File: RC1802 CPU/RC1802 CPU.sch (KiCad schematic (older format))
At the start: 65 parts, among them J1 CONN_01X39, J2 BARREL_JACK, J3 Mount, J4 Mount, J5 Mount, J6 Mount, SW1 CLEAR, SW10 IN5, SW11 IN6, SW12 IN7, SW2 IN, SW3 MP, SW4 WAIT, SW5 IN0, SW6 IN1, SW7 IN2, SW8 IN3, SW9 IN4, U1 CDP1802, U10 MC14495P1, U11 28C256, U2 74LS373, U3 HM62256BLP-7, U4 74LS04, U5 4050, U6 4013, U7 74LS10, U8 MC14495P1, U9 74LS245, X1 CXO_DIP14

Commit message: Placed PCB components (no tracks)
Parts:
- removed AFF1: MSB, Displays_7-Segment:7SegmentLED_LTS6760_LTS6780, symbol LTS-6980HR
- removed AFF2: LSB, Displays_7-Segment:7SegmentLED_LTS6760_LTS6780, symbol LTS-6980HR
- removed C10, C11, C7, C8, C9: 100nF, Capacitors_THT:C_Disc_D4.7mm_W2.5mm_P5.00mm, symbol C_Small
- removed D1: Q LED, LEDs:LED_D5.0mm, symbol LED
- removed D2, D3, D4, D5, D6, D7: 1N4848, Diodes_THT:D_DO-35_SOD27_P7.62mm_Horizontal, symbol D
- removed RN1: 100k, Resistors_THT:R_Array_SIP9, symbol R_Network08
- removed SW1: CLEAR, switches:SPDT_SWITCH, symbol SW_SPDT
- removed SW10: IN5, switches:SPDT_SWITCH, symbol SW_Push_SPDT
- removed SW11: IN6, switches:SPDT_SWITCH, symbol SW_Push_SPDT
- removed SW12: IN7, switches:SPDT_SWITCH, symbol SW_Push_SPDT
- removed SW2: IN, switches:SPDT_PUSH, symbol SW_Push_SPDT
- removed SW3: MP, switches:SPDT_SWITCH, symbol SW_SPDT
- removed SW4: WAIT, switches:SPDT_SWITCH, symbol SW_SPDT
- removed SW5: IN0, switches:SPDT_SWITCH, symbol SW_Push_SPDT
- removed SW6: IN1, switches:SPDT_SWITCH, symbol SW_Push_SPDT
- removed SW7: IN2, switches:SPDT_SWITCH, symbol SW_Push_SPDT
- removed SW8: IN3, switches:SPDT_SWITCH, symbol SW_Push_SPDT
- removed SW9: IN4, switches:SPDT_SWITCH, symbol SW_Push_SPDT
- removed U10, U8: MC14495P1, Housings_DIP:DIP-16_W7.62mm_Socket, symbol MC14495P1
- removed U4: 74LS04, Housings_DIP:DIP-14_W7.62mm_Socket, symbol 74LS04
- removed U5: 4050, Housings_DIP:DIP-16_W7.62mm_Socket, symbol 4050
- removed U6: 4013, Housings_DIP:DIP-14_W7.62mm_Socket, symbol 4013
- removed U7: 74LS10, Housings_DIP:DIP-14_W7.62mm_Socket, symbol 74LS10
- removed U9: 74LS245, Housings_DIP:DIP-20_W7.62mm_Socket, symbol 74HC245
- added D1, D2, D3, D4, D5, D6, D7, D8: LED_Small, LEDs:LED_D5.0mm, symbol LED_Small
- added J6: CONN_02X20, Pin_Headers:Pin_Header_Straight_2x20_Pitch2.54mm, symbol CONN_02X20
- added JP5: SLOT1_WE, Pin_Headers:Pin_Header_Straight_1x03_Pitch2.54mm, symbol Jumper_NC_Dual
- added JP6: BM_OE, Pin_Headers:Pin_Header_Straight_1x03_Pitch2.54mm, symbol Jumper_NC_Dual
- added R11, R12, R13, R14, R15: 220, Resistors_THT:R_Axial_DIN0207_L6.3mm_D2.5mm_P10.16mm_Horizontal, symbol R
- added U1: 74LS04, Housings_DIP:DIP-14_W7.62mm_Socket, symbol 74LS04
- added U3: 74LS240, Housings_DIP:DIP-20_W7.62mm_Socket, symbol 74LS240
- JP4: renamed from JP1; value U12 WE -> SLOT2_WE
- R10: value 470 -> 220
- R8, R9: value 47k -> 220
- U5: renamed from U3; value HM62256BLP-7 -> SLOT-1
- U6: renamed from U11; value 28C256 -> SLOT-2
- renumbered J3 to J1, J4 to J2, J5 to J3, J6 to J4, J1 to J5, J2 to J7, JP2 to JP1, JP3 to JP2, JP4 to JP3, U1 to U2, U2 to U4
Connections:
- net labels added: MP, SLOT1_CS, SLOT2_CS, ~CLEAR, ~WAIT
- net labels removed: CS_RAM, CS_ROM, LOAD_N2, READ, STROBE, ~IN
- wire segments 297 -> 205
- no-connect marks 15 -> 13
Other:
- moved on the sheet: C1, C2, C3, C4, C5, J1, J2, J3, J4, J5, J7, JP1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

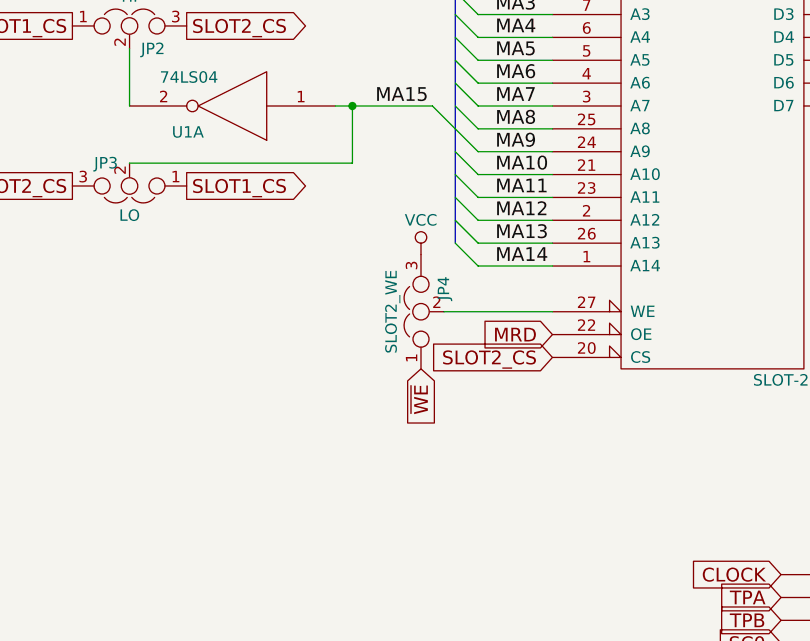
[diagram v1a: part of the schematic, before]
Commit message: All tracks layed out
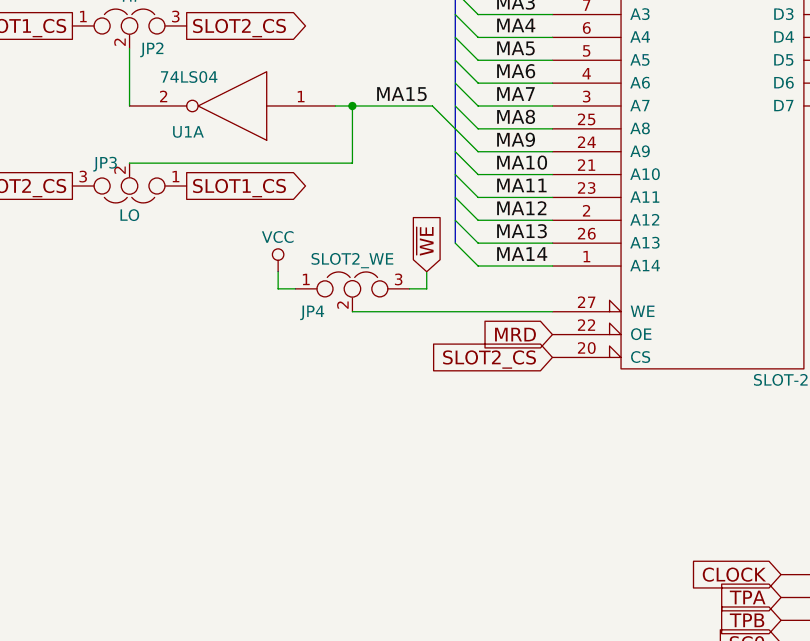
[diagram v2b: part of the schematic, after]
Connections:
- net VCC: now also JP4.1; no longer JP4.3
- net ~WE: now also JP4.3; no longer JP4.1
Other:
- moved on the sheet: JP4
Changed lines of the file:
@@
 L Jumper_NC_Dual JP4
 U 1 1 595437E7
-P 6175 6100
-F 0 "JP4" H 6225 6000 50  0000 L CNN
-F 1 "SLOT2_WE" H 6175 6200 50  0000 C BNN
-F 2 "Pin_Headers:Pin_Header_Straight_1x03_Pitch2.54mm" H 6175 6100 50  0001 C CNN
-F 3 "" H 6175 6100 50  0001 C CNN
-	1    6175 6100
-	0    -1   -1   0
+P 5875 6000
+F 0 "JP4" H 5650 5900 50  0000 L CNN
+F 1 "SLOT2_WE" H 5875 6100 50  0000 C BNN
+F 2 "Pin_Headers:Pin_Header_Straight_1x03_Pitch2.54mm" H 5875 6000 50  0001 C CNN
+F 3 "" H 5875 6000 50  0001 C CNN
+	1    5875 6000
+	1    0    0    -1
 $EndComp
 $Comp
 L VCC #PWR8
 U 1 1 59544DC9
-P 6175 5850
-F 0 "#PWR8" H 6175 5700 50  0001 C CNN
-F 1 "VCC" H 6175 6000 50  0000 C CNN
-F 2 "" H 6175 5850 50  0001 C CNN
-F 3 "" H 6175 5850 50  0001 C CNN
-	1    6175 5850
-	1    0    0    -1
-$EndComp
-Text GLabel 6175 6350 3    60   Input ~ 0
+P 5550 5925
+F 0 "#PWR8" H 5550 5775 50  0001 C CNN
+F 1 "VCC" H 5550 6075 50  0000 C CNN
+F 2 "" H 5550 5925 50  0001 C CNN
+F 3 "" H 5550 5925 50  0001 C CNN
+	1    5550 5925
+	1    0    0    -1
+$EndComp
+Text GLabel 6200 5925 1    60   Input ~ 0
 ~WE
 Text GLabel 15575 6400 0    60   Input ~ 0
@@
 	8750 2600 8525 2600
 Wire Wire Line
-	6275 6100 6750 6100
+	5875 6100 6750 6100
 Wire Wire Line
 	5800 5200 6225 5200
@@
 	11925 1300 11925 1250
 Connection ~ 11650 1300
+Wire Wire Line
+	6200 5925 6200 6000
+Wire Wire Line
+	6200 6000 6125 6000
+Wire Wire Line
+	5550 6000 5625 6000
+Wire Wire Line
+	5550 6000 5550 5925
 $EndSCHEMATC

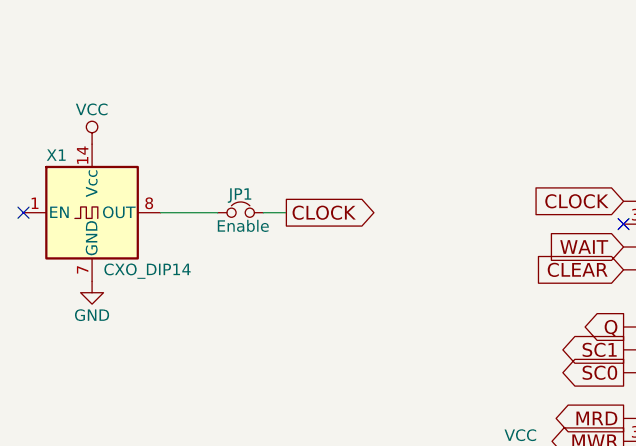
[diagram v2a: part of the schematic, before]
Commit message: Added provisions for using separate clock circuit
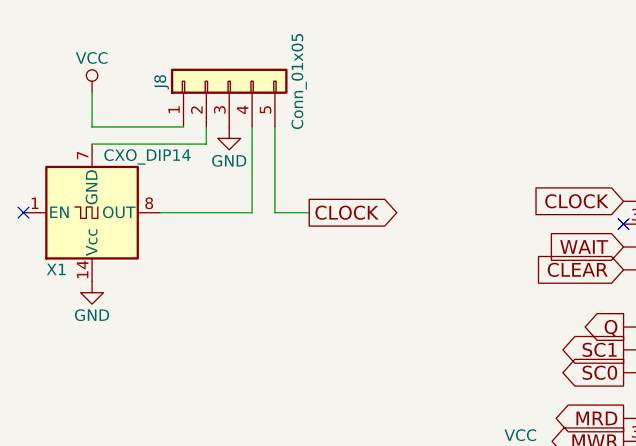
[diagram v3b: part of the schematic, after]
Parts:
- removed JP1: Enable, Pin_Headers:Pin_Header_Straight_1x02_Pitch2.54mm, symbol Jumper_NC_Small
- added J8: Conn_01x05, Pin_Headers:Pin_Header_Straight_1x05_Pitch2.54mm, symbol Conn_01x05
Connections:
- net CLOCK: now also J8.5 (Pin_5)
- net GND: now also X1.14 (Vcc), J8.3 (Pin_3); no longer X1.7 (GND)
- net VCC: now also J8.1 (Pin_1); no longer X1.14 (Vcc)
- net at X1.8 (OUT): now also J8.4 (Pin_4)
- new net: J8.2 (Pin_2), X1.7 (GND)
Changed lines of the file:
@@
 NoConn ~ 3425 1650
 $Comp
-L VCC #PWR21
+L VCC #PWR01
 U 1 1 5946201E
 P 15450 7600
-F 0 "#PWR21" H 15450 7450 50  0001 C CNN
+F 0 "#PWR01" H 15450 7450 50  0001 C CNN
 F 1 "VCC" H 15450 7750 50  0000 C CNN
 F 2 "" H 15450 7600 50  0001 C CNN
@@
 $EndComp
 $Comp
-L GND #PWR20
+L GND #PWR02
 U 1 1 5946208C
 P 15200 7500
-F 0 "#PWR20" H 15200 7250 50  0001 C CNN
+F 0 "#PWR02" H 15200 7250 50  0001 C CNN
 F 1 "GND" H 15200 7350 50  0000 C CNN
 F 2 "" H 15200 7500 50  0001 C CNN
@@
 $EndComp
 $Comp
-L VCC #PWR6
+L VCC #PWR03
 U 1 1 59462274
 P 4225 1075
-F 0 "#PWR6" H 4225 925 50  0001 C CNN
+F 0 "#PWR03" H 4225 925 50  0001 C CNN
 F 1 "VCC" H 4225 1225 50  0000 C CNN
 F 2 "" H 4225 1075 50  0001 C CNN
@@
 $EndComp
 $Comp
-L VCC #PWR7
+L VCC #PWR04
 U 1 1 594628A5
 P 5850 2200
-F 0 "#PWR7" H 5850 2050 50  0001 C CNN
+F 0 "#PWR04" H 5850 2050 50  0001 C CNN
 F 1 "VCC" H 5850 2350 50  0000 C CNN
 F 2 "" H 5850 2200 50  0001 C CNN
@@
 F 3 "" H 1000 1600 50  0001 C CNN
 	1    1100 1600
-	1    0    0    -1
-$EndComp
-$Comp
-L VCC #PWR1
+	1    0    0    1
+$EndComp
+$Comp
+L VCC #PWR05
 U 1 1 59462E75
-P 1100 1300
-F 0 "#PWR1" H 1100 1150 50  0001 C CNN
-F 1 "VCC" H 1100 1450 50  0000 C CNN
-F 2 "" H 1100 1300 50  0001 C CNN
-F 3 "" H 1100 1300 50  0001 C CNN
-	1    1100 1300
-	1    0    0    -1
-$EndComp
-$Comp
-L GND #PWR2
+P 1100 1075
+F 0 "#PWR05" H 1100 925 50  0001 C CNN
+F 1 "VCC" H 1100 1225 50  0000 C CNN
+F 2 "" H 1100 1075 50  0001 C CNN
+F 3 "" H 1100 1075 50  0001 C CNN
+	1    1100 1075
+	1    0    0    -1
+$EndComp
+$Comp
+L GND #PWR06
 U 1 1 59462F59
 P 1100 1900
-F 0 "#PWR2" H 1100 1650 50  0001 C CNN
+F 0 "#PWR06" H 1100 1650 50  0001 C CNN
 F 1 "GND" H 1100 1750 50  0000 C CNN
 F 2 "" H 1100 1900 50  0001 C CNN
@@
 EF4
 $Comp
-L VCC #PWR3
+L VCC #PWR07
 U 1 1 59464C11
 P 2975 2725
-F 0 "#PWR3" H 2975 2575 50  0001 C CNN
+F 0 "#PWR07" H 2975 2575 50  0001 C CNN
 F 1 "VCC" H 2975 2875 50  0000 C CNN
 F 2 "" H 2975 2725 50  0001 C CNN
@@
 TPA
 $Comp
-L GND #PWR9
+L GND #PWR08
 U 1 1 5946BB58
 P 6725 2300
-F 0 "#PWR9" H 6725 2050 50  0001 C CNN
+F 0 "#PWR08" H 6725 2050 50  0001 C CNN
 F 1 "GND" H 6725 2150 50  0000 C CNN
 F 2 "" H 6725 2300 50  0001 C CNN
@@
 BUS
 $Comp
-L GND #PWR5
+L GND #PWR09
 U 1 1 59474506
 P 4125 4300
-F 0 "#PWR5" H 4125 4050 50  0001 C CNN
+F 0 "#PWR09" H 4125 4050 50  0001 C CNN
 F 1 "GND" H 4125 4150 50  0000 C CNN
 F 2 "" H 4125 4300 50  0001 C CNN
@@
 Text Label 8125 2000 0    60   ~ 0
 MA15
-Text GLabel 1950 1600 2    60   Output ~ 0
+Text GLabel 2050 1600 2    60   Output ~ 0
 CLOCK
 Text GLabel 3425 1550 0    60   Input ~ 0
@@
 $EndComp
 $Comp
-L VCC #PWR8
+L VCC #PWR010
 U 1 1 59544DC9
 P 5550 5925
-F 0 "#PWR8" H 5550 5775 50  0001 C CNN
+F 0 "#PWR010" H 5550 5775 50  0001 C CNN
 F 1 "VCC" H 5550 6075 50  0000 C CNN
 F 2 "" H 5550 5925 50  0001 C CNN
@@
 SLOT1_CS
 $Comp
-L Jumper_NC_Small JP1
-U 1 1 5958558E
-P 1750 1600
-F 0 "JP1" H 1750 1680 50  0000 C CNN
-F 1 "Enable" H 1760 1540 50  0000 C CNN
-F 2 "Pin_Headers:Pin_Header_Straight_1x02_Pitch2.54mm" H 1750 1600 50  0001 C CNN
-F 3 "" H 1750 1600 50  0001 C CNN
-	1    1750 1600
-	1    0    0    -1
-$EndComp
-$Comp
 L C_Small C1
 U 1 1 595CF017
@@
 $EndComp
 $Comp
-L VCC #PWR14
+L VCC #PWR011
 U 1 1 595D67C5
 P 10550 950
-F 0 "#PWR14" H 10550 800 50  0001 C CNN
+F 0 "#PWR011" H 10550 800 50  0001 C CNN
 F 1 "VCC" H 10550 1100 50  0000 C CNN
 F 2 "" H 10550 950 50  0001 C CNN
@@
 $EndComp
 $Comp
-L GND #PWR15
+L GND #PWR012
 U 1 1 595D6DCD
 P 10550 1350
-F 0 "#PWR15" H 10550 1100 50  0001 C CNN
+F 0 "#PWR012" H 10550 1100 50  0001 C CNN
 F 1 "GND" H 10550 1200 50  0000 C CNN
 F 2 "" H 10550 1350 50  0001 C CNN
@@
 $EndComp
 $Comp
-L VCC #PWR22
+L VCC #PWR013
 U 1 1 595E10E8
 P 15575 1025
-F 0 "#PWR22" H 15575 875 50  0001 C CNN
+F 0 "#PWR013" H 15575 875 50  0001 C CNN
 F 1 "VCC" H 15575 1175 50  0000 C CNN
 F 2 "" H 15575 1025 50  0001 C CNN
@@
 $EndComp
 $Comp
-L GND #PWR23
+L GND #PWR014
 U 1 1 595E22B1
 P 15575 1400
-F 0 "#PWR23" H 15575 1150 50  0001 C CNN
+F 0 "#PWR014" H 15575 1150 50  0001 C CNN
 F 1 "GND" H 15575 1250 50  0000 C CNN
 F 2 "" H 15575 1400 50  0001 C CNN
@@
 	8125 2000 8325 2000
 Wire Wire Line
-	1400 1600 1650 1600
+	1400 1600 1800 1600
 Wire Bus Line
 	15050 8325 14850 8325
@@
 Wire Wire Line
 	4900 5450 5875 5450
-Wire Wire Line
-	1850 1600 1950 1600
 Wire Wire Line
 	10550 950  10550 1050
@@
 DMA_IN
 $Comp
-L VCC #PWR18
+L VCC #PWR015
 U 1 1 5987AAE8
 P 12875 3425
-F 0 "#PWR18" H 12875 3275 50  0001 C CNN
+F 0 "#PWR015" H 12875 3275 50  0001 C CNN
 F 1 "VCC" H 12875 3575 50  0000 C CNN
 F 2 "" H 12875 3425 50  0001 C CNN
@@
 $EndComp
 $Comp
-L GND #PWR19
+L GND #PWR016
 U 1 1 5987AAE9
 P 12950 5400
-F 0 "#PWR19" H 12950 5150 50  0001 C CNN
+F 0 "#PWR016" H 12950 5150 50  0001 C CNN
 F 1 "GND" H 12950 5250 50  0000 C CNN
 F 2 "" H 12950 5400 50  0001 C CNN
@@
 Connection ~ 1550 10000
 $Comp
-L GND #PWR4
+L GND #PWR017
 U 1 1 5B2329DF
 P 3000 10150
-F 0 "#PWR4" H 3000 9900 50  0001 C CNN
+F 0 "#PWR017" H 3000 9900 50  0001 C CNN
 F 1 "GND" H 3000 10000 50  0000 C CNN
 F 2 "" H 3000 10150 50  0001 C CNN
@@
 $EndComp
 $Comp
-L VCC #PWR12
+L VCC #PWR018
 U 1 1 5B230CC5
 P 8850 3300
-F 0 "#PWR12" H 8850 3150 50  0001 C CNN
+F 0 "#PWR018" H 8850 3150 50  0001 C CNN
 F 1 "VCC" H 8850 3450 50  0000 C CNN
 F 2 "" H 8850 3300 50  0001 C CNN
@@
 Connection ~ 7675 8200
 $Comp
-L VCC #PWR10
+L VCC #PWR019
 U 1 1 5B238BC7
 P 7275 8350
-F 0 "#PWR10" H 7275 8200 50  0001 C CNN
+F 0 "#PWR019" H 7275 8200 50  0001 C CNN
 F 1 "VCC" H 7275 8500 50  0000 C CNN
 F 2 "" H 7275 8350 50  0001 C CNN
@@
 $EndComp
 $Comp
-L GND #PWR11
+L GND #PWR020
 U 1 1 5B238E91
 P 7775 8350
-F 0 "#PWR11" H 7775 8100 50  0001 C CNN
+F 0 "#PWR020" H 7775 8100 50  0001 C CNN
 F 1 "GND" H 7775 8200 50  0000 C CNN
 F 2 "" H 7775 8350 50  0001 C CNN
@@
 $EndComp
 $Comp
-L GND #PWR13
+L GND #PWR021
 U 1 1 5B244389
 P 9725 8025
-F 0 "#PWR13" H 9725 7775 50  0001 C CNN
+F 0 "#PWR021" H 9725 7775 50  0001 C CNN
 F 1 "GND" H 9725 7875 50  0000 C CNN
 F 2 "" H 9725 8025 50  0001 C CNN
@@
 Wire Wire Line
 	5550 6000 5550 5925
+Wire Wire Line
+	1100 1300 1600 1300
+Wire Wire Line
+	1600 1300 1600 1225
+Wire Wire Line
+	1500 1225 1100 1225
+Wire Wire Line
+	1100 1225 1100 1075
+$Comp
+L Conn_01x05 J8
+U 1 1 5B2BCE80
+P 1700 1025
+F 0 "J8" H 1700 1325 50  0000 C CNN
+F 1 "Conn_01x05" H 1700 725 50  0000 C CNN
+F 2 "Pin_Headers:Pin_Header_Straight_1x05_Pitch2.54mm" H 1700 1025 50  0001 C CNN
+F 3 "" H 1700 1025 50  0001 C CNN
+	1    1700 1025
+	0    -1   -1   0
+$EndComp
+Wire Wire Line
+	1900 1225 1900 1600
+Wire Wire Line
+	1900 1600 2050 1600
+Wire Wire Line
+	1800 1600 1800 1225
+$Comp
+L GND #PWR022
+U 1 1 5B2BD472
+P 1700 1225
+F 0 "#PWR022" H 1700 975 50  0001 C CNN
+F 1 "GND" H 1700 1075 50  0000 C CNN
+F 2 "" H 1700 1225 50  0001 C CNN
+F 3 "" H 1700 1225 50  0001 C CNN
+	1    1700 1225
+	1    0    0    -1
+$EndComp
 $EndSCHEMATC

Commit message: Fixed stupid socket pin count mistake
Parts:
- U5, U6: footprint Housings_DIP:DIP-32_W15.24mm_Socket -> Housings_DIP:DIP-28_W15.24mm_Socket
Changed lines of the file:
@@
 F 0 "U5" H 7125 4250 50  0000 C CNN
 F 1 "SLOT-1" H 7825 2550 50  0000 C CNN
-F 2 "Housings_DIP:DIP-32_W15.24mm_Socket" H 7425 3350 50  0001 C CIN
+F 2 "Housings_DIP:DIP-28_W15.24mm_Socket" H 7425 3350 50  0001 C CIN
 F 3 "" H 7425 3350 50  0001 C CNN
 	1    7425 3350
@@
 F 0 "U6" H 7650 6400 50  0000 C CNN
 F 1 "SLOT-2" H 7750 4400 50  0000 C CNN
-F 2 "Housings_DIP:DIP-32_W15.24mm_Socket" H 7450 5400 50  0001 C CNN
+F 2 "Housings_DIP:DIP-28_W15.24mm_Socket" H 7450 5400 50  0001 C CNN
 F 3 "" H 7450 5400 50  0001 C CNN
 	1    7450 5400

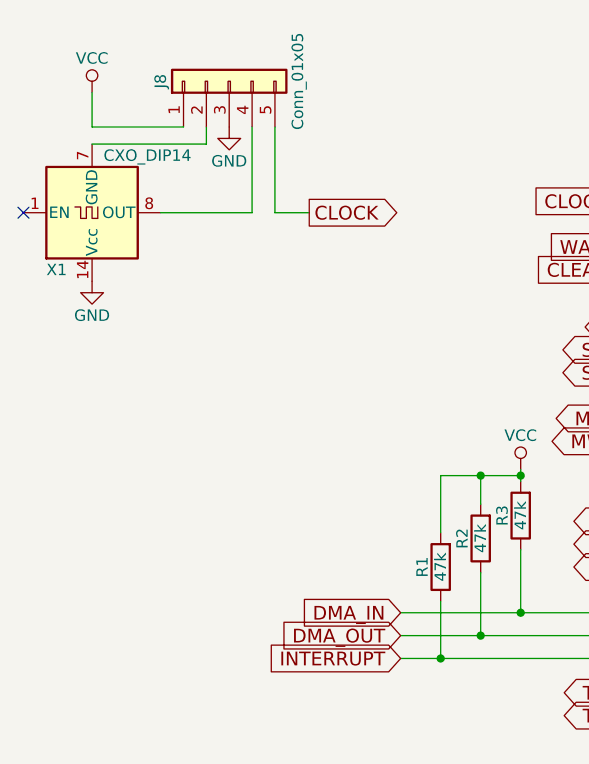
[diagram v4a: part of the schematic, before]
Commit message: Added Q connector and some silksceen info
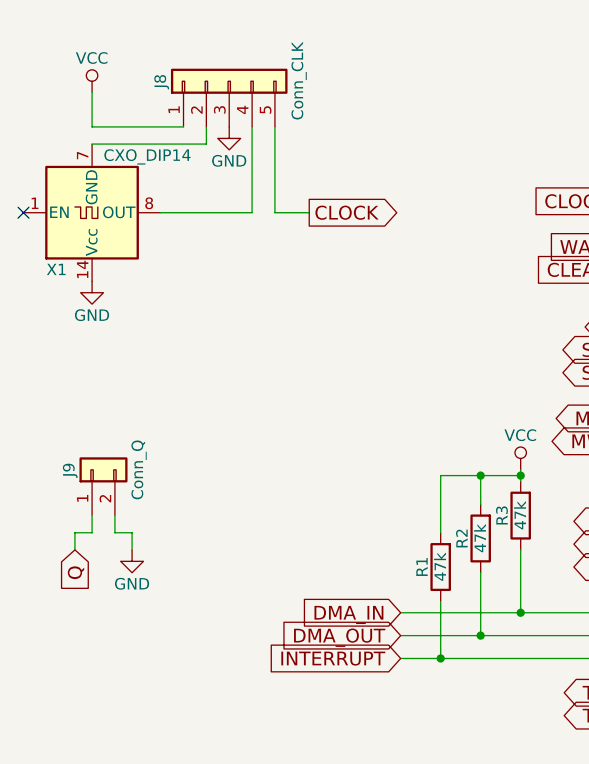
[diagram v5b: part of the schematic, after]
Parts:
- added J9: Conn_Q, Pin_Headers:Pin_Header_Angled_1x02_Pitch2.54mm, symbol Conn_01x02
- J8: value Conn_01x05 -> Conn_CLK
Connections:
- net GND: now also J9.2 (Pin_2)
- net Q: now also J9.1 (Pin_1)
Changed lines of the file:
@@
 P 1700 1025
 F 0 "J8" H 1700 1325 50  0000 C CNN
-F 1 "Conn_01x05" H 1700 725 50  0000 C CNN
+F 1 "Conn_CLK" H 1700 725 50  0000 C CNN
 F 2 "Pin_Headers:Pin_Header_Straight_1x05_Pitch2.54mm" H 1700 1025 50  0001 C CNN
 F 3 "" H 1700 1025 50  0001 C CNN
@@
 	1    0    0    -1
 $EndComp
+$Comp
+L Conn_01x02 J9
+U 1 1 5B6A11D6
+P 1100 2725
+F 0 "J9" H 1100 2825 50  0000 C CNN
+F 1 "Conn_Q" H 1100 2525 50  0000 C CNN
+F 2 "Pin_Headers:Pin_Header_Angled_1x02_Pitch2.54mm" H 1100 2725 50  0001 C CNN
+F 3 "" H 1100 2725 50  0001 C CNN
+	1    1100 2725
+	0    -1   -1   0
+$EndComp
+Text GLabel 1025 3075 3    60   Input ~ 0
+Q
+$Comp
+L GND #PWR023
+U 1 1 5B6A17C7
+P 1275 3075
+F 0 "#PWR023" H 1275 2825 50  0001 C CNN
+F 1 "GND" H 1275 2925 50  0000 C CNN
+F 2 "" H 1275 3075 50  0001 C CNN
+F 3 "" H 1275 3075 50  0001 C CNN
+	1    1275 3075
+	1    0    0    -1
+$EndComp
+Wire Wire Line
+	1025 3075 1025 3000
+Wire Wire Line
+	1025 3000 1100 3000
+Wire Wire Line
+	1100 3000 1100 2925
+Wire Wire Line
+	1200 2925 1200 3000
+Wire Wire Line
+	1275 3075 1275 3000
+Wire Wire Line
+	1275 3000 1200 3000
 $EndSCHEMATC

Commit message: Q connector now 4 pins to match speaker and TTL serial
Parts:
- J9: footprint Pin_Headers:Pin_Header_Angled_1x02_Pitch2.54mm -> Pin_Headers:Pin_Header_Angled_1x04_Pitch2.54mm; symbol Conn_01x02 -> Conn_01x04
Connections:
- net EF3: now also J9.3 (Pin_3)
- net GND: now also J9.4 (Pin_4); no longer J9.2 (Pin_2)
- net VCC: now also J9.2 (Pin_2)
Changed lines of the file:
@@
 $EndComp
 $Comp
-L Conn_01x02 J9
+L Conn_01x04 J9
 U 1 1 5B6A11D6
 P 1100 2725
 F 0 "J9" H 1100 2825 50  0000 C CNN
 F 1 "Conn_Q" H 1100 2525 50  0000 C CNN
-F 2 "Pin_Headers:Pin_Header_Angled_1x02_Pitch2.54mm" H 1100 2725 50  0001 C CNN
+F 2 "Pin_Headers:Pin_Header_Angled_1x04_Pitch2.54mm" H 1100 2725 50  0001 C CNN
 F 3 "" H 1100 2725 50  0001 C CNN
 	1    1100 2725
 	0    -1   -1   0
 $EndComp
-Text GLabel 1025 3075 3    60   Input ~ 0
+Text GLabel 925  3075 3    60   Input ~ 0
 Q
 $Comp
 L GND #PWR023
 U 1 1 5B6A17C7
-P 1275 3075
-F 0 "#PWR023" H 1275 2825 50  0001 C CNN
-F 1 "GND" H 1275 2925 50  0000 C CNN
-F 2 "" H 1275 3075 50  0001 C CNN
-F 3 "" H 1275 3075 50  0001 C CNN
-	1    1275 3075
+P 1375 3075
+F 0 "#PWR023" H 1375 2825 50  0001 C CNN
+F 1 "GND" H 1375 2925 50  0000 C CNN
+F 2 "" H 1375 3075 50  0001 C CNN
+F 3 "" H 1375 3075 50  0001 C CNN
+	1    1375 3075
 	1    0    0    -1
 $EndComp
 Wire Wire Line
-	1025 3075 1025 3000
+	925  3075 925  3000
 Wire Wire Line
-	1025 3000 1100 3000
+	925  3000 1000 3000
 Wire Wire Line
-	1100 3000 1100 2925
+	1000 3000 1000 2925
+Wire Wire Line
+	1300 2925 1300 3000
+Wire Wire Line
+	1375 3075 1375 3000
+Wire Wire Line
+	1375 3000 1300 3000
+$Comp
+L VCC #PWR024
+U 1 1 5B6A3EEC
+P 1100 3200
+F 0 "#PWR024" H 1100 3050 50  0001 C CNN
+F 1 "VCC" H 1100 3350 50  0000 C CNN
+F 2 "" H 1100 3200 50  0001 C CNN
+F 3 "" H 1100 3200 50  0001 C CNN
+	1    1100 3200
+	-1   0    0    1
+$EndComp
+Wire Wire Line
+	1100 2925 1100 3200
+Text GLabel 1200 3000 3    60   Input ~ 0
+EF3
 Wire Wire Line
 	1200 2925 1200 3000
-Wire Wire Line
-	1275 3075 1275 3000
-Wire Wire Line
-	1275 3000 1200 3000
 $EndSCHEMATC
